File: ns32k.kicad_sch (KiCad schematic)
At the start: 49 parts, among them SW2 SW_DIP_x04, U1 NS32201, U10 74AHC373, U11 74AHC373, U12 74AHC138, U13 AS6C6416-55, U15 MX29LV040C, U16 MX29LV040C, U19 74AHC138, U20 74AHC1G08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

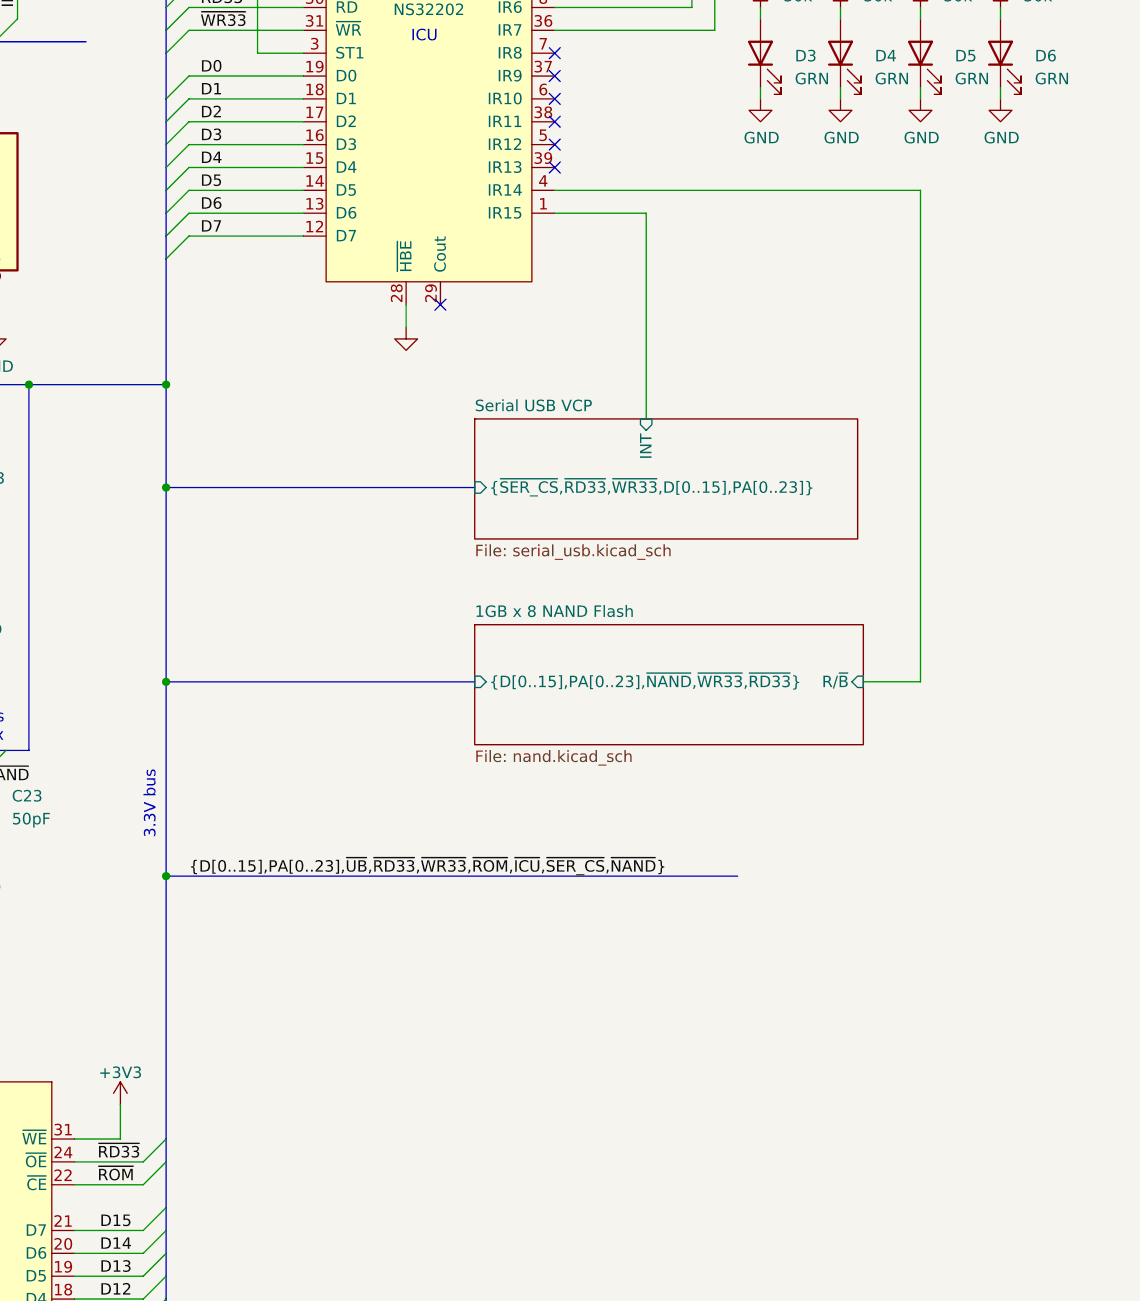
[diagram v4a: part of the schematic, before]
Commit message: add ethernet to schematic
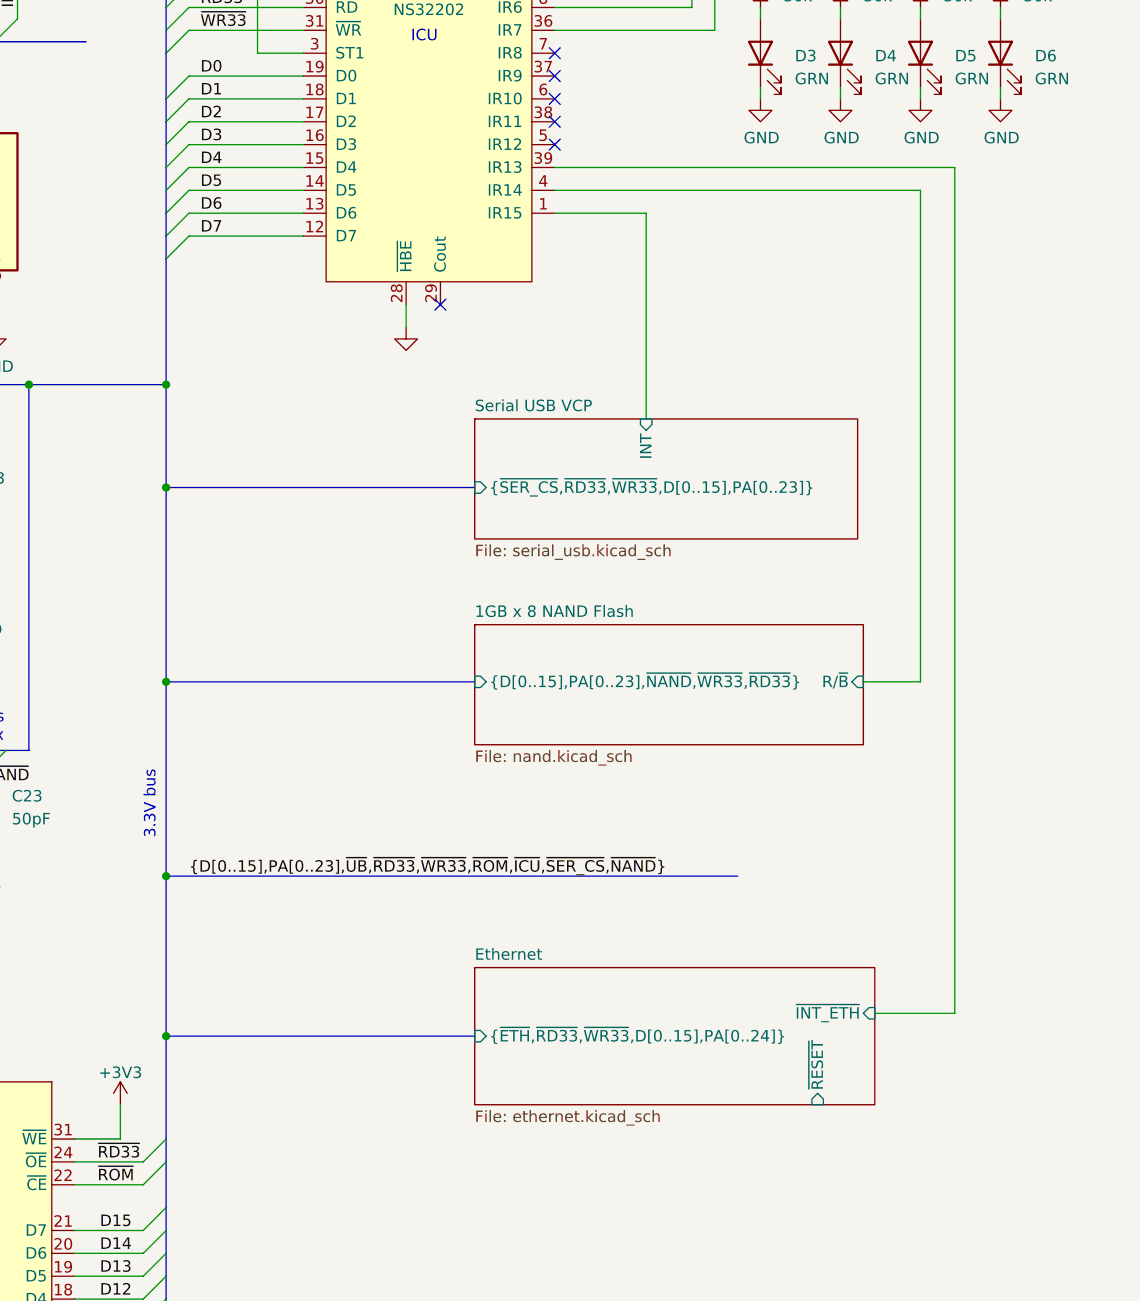
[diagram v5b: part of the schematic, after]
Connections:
- net Ethernet/~{INT_ETH}: now reaches U5.39 (IR13)
- no-connect marks 21 -> 20
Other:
- added sheet Ethernet (ethernet.kicad_sch)
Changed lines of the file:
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@@
 	)
 	(junction
+		(at 293.37 186.69)
+		(diameter 0)
+		(color 0 0 0 0)
+	)
+	(junction
 		(at 30.48 237.49)
 		(diameter 0)
@@
 	)
 	(no_connect
-		(at 336.55 90.17)
-	)
-	(no_connect
 		(at 336.55 87.63)
 	)
@@
 		)
 	)
+	(wire
+		(pts
+			(xy 336.55 90.17) (xy 381 90.17)
+		)
+		(stroke
+			(width 0)
+			(type default)
+		)
+	)
 	(bus
 		(pts
@@
 		)
 	)
+	(bus
+		(pts
+			(xy 293.37 186.69) (xy 327.66 186.69)
+		)
+		(stroke
+			(width 0)
+			(type default)
+		)
+	)
 	(wire
 		(pts
@@
 	(bus
 		(pts
-			(xy 293.37 168.91) (xy 293.37 198.12)
+			(xy 293.37 168.91) (xy 293.37 186.69)
 		)
 		(stroke
@@
 		)
 	)
+	(bus
+		(pts
+			(xy 293.37 186.69) (xy 293.37 198.12)
+		)
+		(stroke
+			(width 0)
+			(type default)
+		)
+	)
 	(wire
 		(pts
@@
 		)
 	)
+	(wire
+		(pts
+			(xy 381 184.15) (xy 372.11 184.15)
+		)
+		(stroke
+			(width 0)
+			(type default)
+		)
+	)
 	(bus
 		(pts
@@
 		)
 	)
+	(wire
+		(pts
+			(xy 381 90.17) (xy 381 184.15)
+		)
+		(stroke
+			(width 0)
+			(type default)
+		)
+	)
 	(bus
 		(pts
@@
 				)
 			)
+		)
+	)
+	(sheet
+		(at 327.66 179.07)
+		(size 44.45 15.24)
+		(fields_autoplaced yes)
+		(stroke
+			(width 0.1524)
+			(type solid)
+		)
+		(fill
+			(color 0 0 0 0.0000)
+		)
+		(property "Sheetname" "Ethernet"
+			(at 327.66 178.3584 0)
+			(effects
+				(font
+					(size 1.27 1.27)
+				)
+				(justify left bottom)
+			)
+		)
+		(property "Sheetfile" "ethernet.kicad_sch"
+			(at 327.66 194.8946 0)
+			(effects
+				(font
+					(size 1.27 1.27)
+				)
+				(justify left top)
+			)
+		)
+		(pin "~{INT_ETH}" input
+			(at 372.11 184.15 0)
+			(effects
+				(font
+					(size 1.27 1.27)
+				)
+				(justify right)
+			)
+		)
+		(pin "{~{ETH},~{RD33},~{WR33},D[0..15],PA[0..24]}" input
+			(at 327.66 186.69 180)
+			(effects
+				(font
+					(size 1.27 1.27)
+				)
+				(justify left)
+			)
+		)
+		(pin "~{RESET}" input
+			(at 365.76 194.31 270)
+			(effects
+				(font
+					(size 1.27 1.27)
+				)
+				(justify left)
+			)
+		)
+		(instances
+			(project "ns32k"
+				(path "/54787df0-1b8c-465f-acae-f55ec7f02da3"
+					(page "5")
+				)
+			)

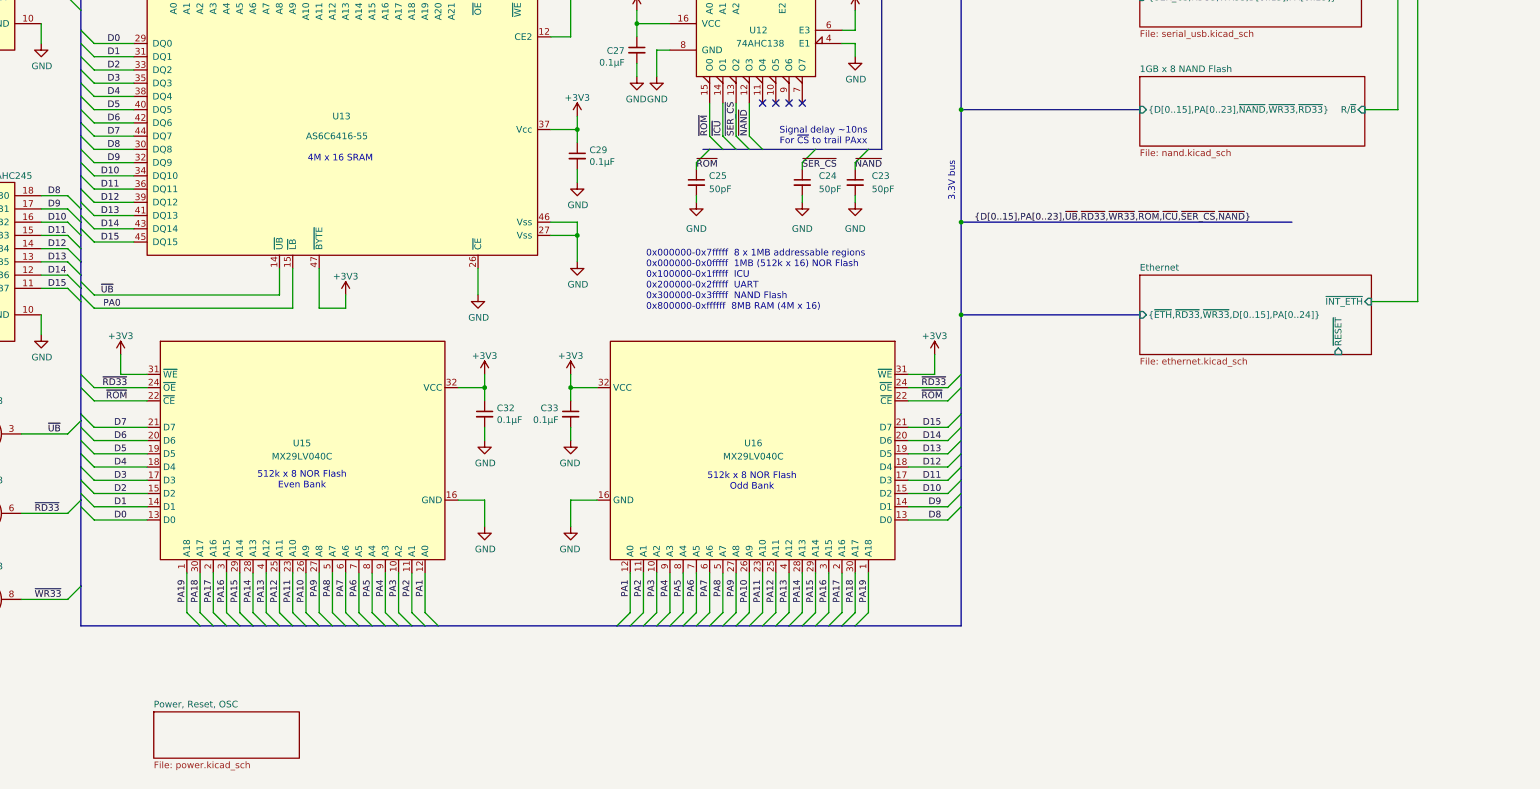
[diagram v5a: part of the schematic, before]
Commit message: fix DRC errors, add RJ45 step model
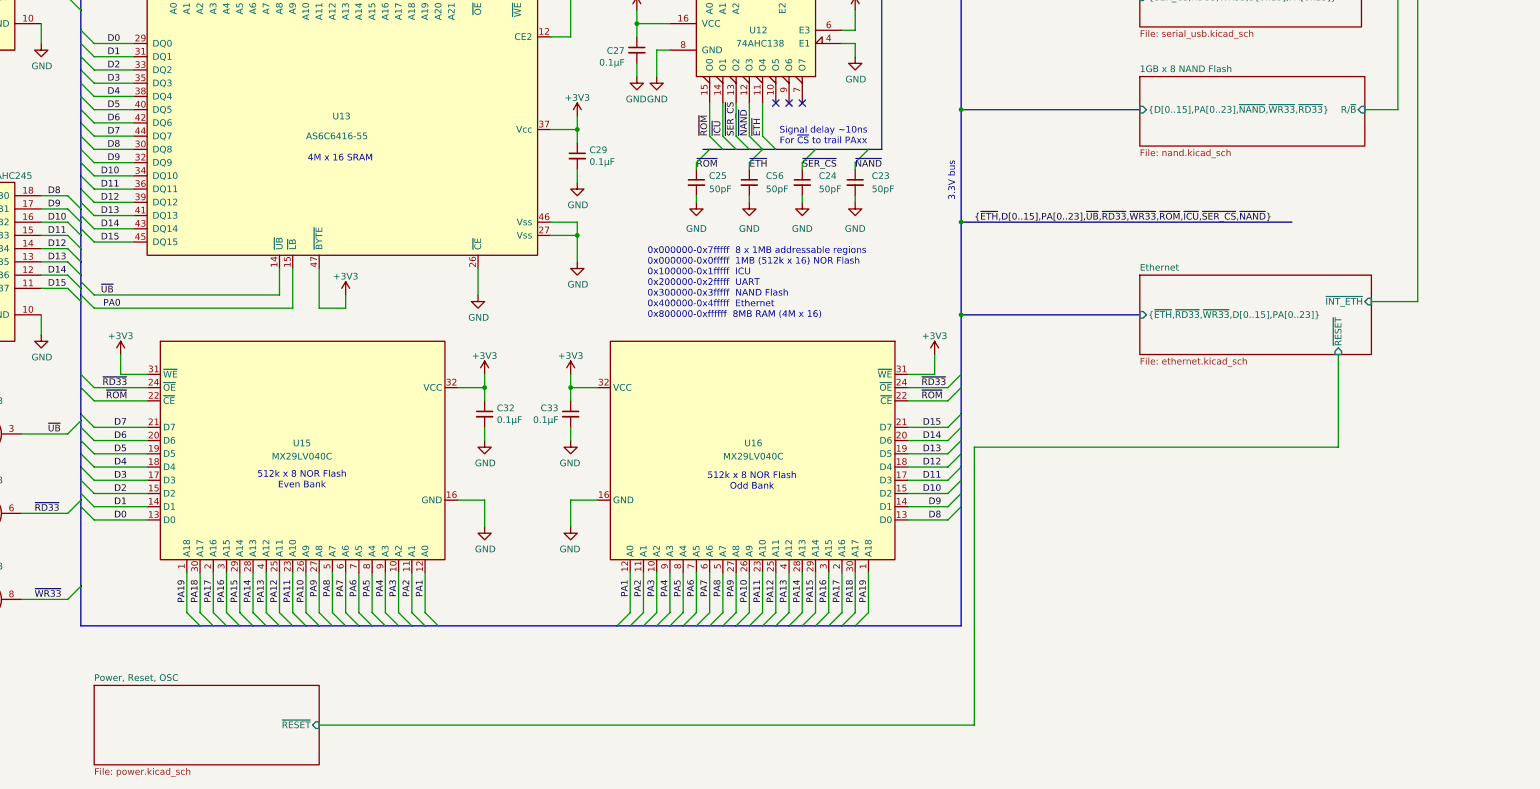
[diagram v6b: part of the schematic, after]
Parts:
- added C56: 50pF, Capacitor_SMD:C_0402_1005Metric, symbol Device:C_Small
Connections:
- net GND: now also C56.2
- net ~{ETH}: now reaches U12.11 (O4)
- net ~{ETH}: now also C56.1
- no-connect marks 20 -> 19
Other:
- sheet Ethernet ports: added {~{ETH},~{RD33},~{WR33},D[0..15],PA[0..23]}; removed {~{ETH},~{RD33},~{WR33},D[0..15],PA[0..24]}
- sheet Power, Reset, OSC ports: added ~{RESET}; removed none
- note added: "0x000000-0x7fffff 8 x 1MB addressable regions 0x000000-0x0fffff 1MB (512k x 16) NOR Flash 0x100000-0x1fffff ICU 0x200000-0x2fffff UART 0x300000-0x3fffff NAND Flash 0x400000-0x4fffff Ethernet 0x800000-0xffffff 8MB RAM (4M x 16)"
- note removed: "0x000000-0x7fffff 8 x 1MB addressable regions 0x000000-0x0fffff 1MB (512k x 16) NOR Flash 0x100000-0x1fffff ICU 0x200000-0x2fffff UART 0x300000-0x3fffff NAND Flash 0x800000-0xffffff 8MB RAM (4M x 16)"
